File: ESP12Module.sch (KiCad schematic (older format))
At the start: 19 parts, among them J1 Conn_01x05_Male, J2 Conn_01x05_Male, J3 Screw_Terminal_01x02, J4 Conn_01x02_Male, SW4 SW_Push, U2 ESP-12S, sw3 SW_Push

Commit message: Added amp
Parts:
- added U?: IR4301, Package_DFN_QFN:Infineon_PQFN-22-15-4EP_6x5mm_P0.65mm, symbol Amplifier_Audio:IR4301
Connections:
- new net: U?.15 (COM), U?.9 (COM)
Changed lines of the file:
@@
 	7950 3750 7950 3850
 Connection ~ 7950 3850
+$Comp
+L Amplifier_Audio:IR4301 U?
+U 1 1 5F6871D4
+P 3450 3675
+F 0 "U?" H 3450 4656 50  0000 C CNN
+F 1 "IR4301" H 3450 4565 50  0000 C CNN
+F 2 "Package_DFN_QFN:Infineon_PQFN-22-15-4EP_6x5mm_P0.65mm" H 3450 3675 50  0001 C CIN
+F 3 "https://www.infineon.com/dgdl/ir4301.pdf?fileId=5546d462533600a4015355d5fc691819" H 3450 3675 50  0001 C CNN
+	1    3450 3675
+	1    0    0    -1
+$EndComp
 $EndSCHEMATC

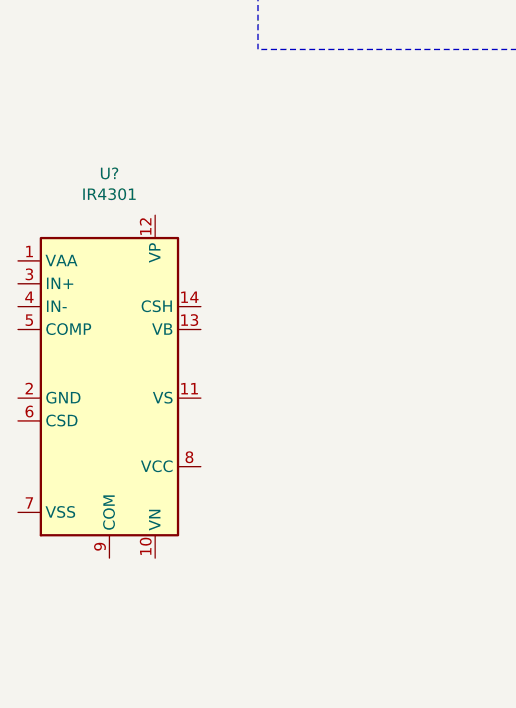
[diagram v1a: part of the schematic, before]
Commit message: Deleted amp
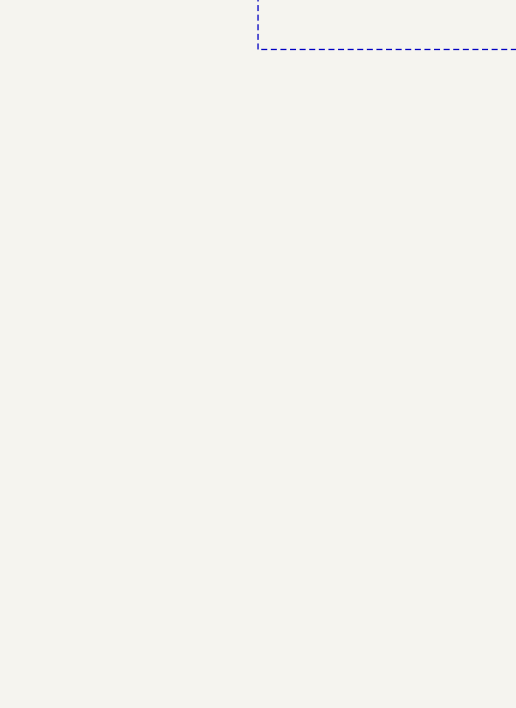
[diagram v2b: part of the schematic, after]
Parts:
- removed U?: IR4301, Package_DFN_QFN:Infineon_PQFN-22-15-4EP_6x5mm_P0.65mm, symbol Amplifier_Audio:IR4301
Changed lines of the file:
@@
 	7950 3750 7950 3850
 Connection ~ 7950 3850
-$Comp
-L Amplifier_Audio:IR4301 U?
-U 1 1 5F6871D4
-P 3450 3675
-F 0 "U?" H 3450 4656 50  0000 C CNN
-F 1 "IR4301" H 3450 4565 50  0000 C CNN
-F 2 "Package_DFN_QFN:Infineon_PQFN-22-15-4EP_6x5mm_P0.65mm" H 3450 3675 50  0001 C CIN
-F 3 "https://www.infineon.com/dgdl/ir4301.pdf?fileId=5546d462533600a4015355d5fc691819" H 3450 3675 50  0001 C CNN
-	1    3450 3675
-	1    0    0    -1
-$EndComp
 $EndSCHEMATC
